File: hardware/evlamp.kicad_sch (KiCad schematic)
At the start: 21 parts

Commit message: update KiCad project
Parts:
- added C2: (no value), symbol GOST_Capacitors:CAPACITOR_POLAR
- C1: value (none) -> 1,0; footprint (none) -> Capacitor_SMD:C_0805_2012Metric_Pad1.18x1.45mm_HandSolder
- X1: footprint (none) -> TerminalBlock:TerminalBlock_bornier-3_P5.08mm
- X11: footprint (none) -> Connector_PinHeader_2.54mm:PinHeader_1x03_P2.54mm_Vertical
- X2: footprint (none) -> TerminalBlock:TerminalBlock_bornier-2_P5.08mm
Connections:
- net +5V: now also C2.1
- net GND: now also C2.2
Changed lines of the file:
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@@
   (junction (at 72.39 114.3) (diameter 0) (color 0 0 0 0)
+  )
+  (junction (at 64.77 106.68) (diameter 0) (color 0 0 0 0)
   )
   (junction (at 72.39 111.76) (diameter 0) (color 0 0 0 0)
@@
     (stroke (width 0) (type default) (color 0 0 0 0))
   )
+  (wire (pts (xy 64.77 106.68) (xy 72.39 106.68))
+    (stroke (width 0) (type default) (color 0 0 0 0))
+  )
   (wire (pts (xy 182.88 76.2) (xy 191.77 76.2))
     (stroke (width 0) (type default) (color 0 0 0 0))
@@
     (stroke (width 0) (type default) (color 0 0 0 0))
   )
+  (wire (pts (xy 62.23 106.68) (xy 64.77 106.68))
+    (stroke (width 0) (type default) (color 0 0 0 0))
+  )
   (wire (pts (xy 124.46 99.06) (xy 129.54 99.06))
     (stroke (width 0) (type default) (color 0 0 0 0))
@@
   )
   (wire (pts (xy 172.72 106.68) (xy 175.26 106.68))
+    (stroke (width 0) (type default) (color 0 0 0 0))
+  )
+  (wire (pts (xy 64.77 106.68) (xy 64.77 109.22))
     (stroke (width 0) (type default) (color 0 0 0 0))
   )
@@
     (pin "1")
   )
-  (symbol (lib_id "GOST_Power_Symbols:+5V") (at 72.39 106.68 90) (unit 1)
-    (in_bom yes) (on_board yes)
-    (property "Reference" "#PWR0102" (id 0) (at 73.152 106.68 0)
-      (effects (font (size 1.27 1.27)) (justify top) hide)
-    )
-    (property "Value" "+5V" (id 1) (at 69.215 106.68 90)
-      (effects (font (size 1.27 1.27)) (justify left))
-    )
-    (property "Footprint" "" (id 2) (at 72.39 106.68 0)
-      (effects (font (size 0 0)) hide)
-    )
-    (property "Datasheet" "" (id 3) (at 72.39 106.68 0)
+  (symbol (lib_id "GOST_Power_Symbols:+5V") (at 62.23 106.68 90) (unit 1)
+    (in_bom yes) (on_board yes)
+    (property "Reference" "#PWR0102" (id 0) (at 62.992 106.68 0)
+      (effects (font (size 1.27 1.27)) (justify top) hide)
+    )
+    (property "Value" "+5V" (id 1) (at 59.055 106.68 90)
+      (effects (font (size 1.27 1.27)) (justify left))
+    )
+    (property "Footprint" "" (id 2) (at 62.23 106.68 0)
+      (effects (font (size 0 0)) hide)
+    )
+    (property "Datasheet" "" (id 3) (at 62.23 106.68 0)
       (effects (font (size 1.27 1.27)) hide)
     )
@@
     (property "Reference" "X2" (id 0) (at 208.28 37.465 0))
     (property "Value" "" (id 1) (at 208.28 40.005 0))
-    (property "Footprint" "" (id 2) (at 208.915 37.465 0)
+    (property "Footprint" "TerminalBlock:TerminalBlock_bornier-2_P5.08mm" (id 2) (at 208.915 37.465 0)
       (effects (font (size 1.27 1.27)) hide)
     )
@@
     (property "Reference" "X11" (id 0) (at 256.54 51.435 0))
     (property "Value" "" (id 1) (at 256.54 53.975 0))
-    (property "Footprint" "" (id 2) (at 257.175 51.435 0)
+    (property "Footprint" "Connector_PinHeader_2.54mm:PinHeader_1x03_P2.54mm_Vertical" (id 2) (at 257.175 51.435 0)
       (effects (font (size 1.27 1.27)) hide)
     )
@@
       (effects (font (size 1.27 1.27)) (justify top) hide)
     )
-    (property "Value" "" (id 1) (at 69.215 104.14 90)
+    (property "Value" "+3V3" (id 1) (at 69.215 104.14 90)
       (effects (font (size 1.27 1.27)) (justify left))
     )
@@
     (property "Reference" "X1" (id 0) (at 208.28 17.145 0))
     (property "Value" "" (id 1) (at 208.28 19.685 0))
-    (property "Footprint" "" (id 2) (at 208.915 17.145 0)
+    (property "Footprint" "TerminalBlock:TerminalBlock_bornier-3_P5.08mm" (id 2) (at 208.915 17.145 0)
       (effects (font (size 1.27 1.27)) hide)
     )
@@
     (pin "2")
   )
+  (symbol (lib_id "GOST_Capacitors:CAPACITOR_POLAR") (at 64.77 111.76 270) (unit 1)
+    (in_bom yes) (on_board yes) (fields_autoplaced)
+    (property "Reference" "C2" (id 0) (at 61.9506 110.1506 90)
+      (effects (font (size 1.27 1.27)) (justify right))
+    )
+    (property "Value" "" (id 1) (at 61.9506 112.6875 90)
+      (effects (font (size 1.27 1.27)) (justify right))
+    )
+    (property "Footprint" "" (id 2) (at 64.77 111.76 0)
+      (effects (font (size 0 0)) hide)
+    )
+    (property "Datasheet" "" (id 3) (at 64.77 111.76 0)
+      (effects (font (size 1.27 1.27)) hide)
+    )
+    (pin "1")
+    (pin "2")
+  )
   (symbol (lib_id "GOST_Power_Symbols:GND") (at 191.77 78.74 0) (unit 1)
     (in_bom yes) (on_board yes)
@@
       (effects (font (size 1.27 1.27)) (justify bottom))
     )
-    (property "Value" "" (id 1) (at 67.31 63.754 0)
+    (property "Value" "1,0" (id 1) (at 67.31 63.754 0)
       (effects (font (size 1.27 1.27)) (justify top))
     )
-    (property "Footprint" "" (id 2) (at 67.31 60.96 0)
+    (property "Footprint" "Capacitor_SMD:C_0805_2012Metric_Pad1.18x1.45mm_HandSolder" (id 2) (at 67.31 60.96 0)
       (effects (font (size 0 0)) hide)
     )
@@
     (pin "1")
   )
+  (symbol (lib_id "GOST_Power_Symbols:GND") (at 64.77 114.3 0) (unit 1)
+    (in_bom yes) (on_board yes)
+    (property "Reference" "#PWR01" (id 0) (at 64.77 113.538 0)
+      (effects (font (size 1.27 1.27)) (justify bottom) hide)
+    )
+    (property "Value" "GND" (id 1) (at 64.77 117.602 0)
+      (effects (font (size 1.27 1.27)) (justify top) hide)
+    )
+    (property "Footprint" "" (id 2) (at 64.77 114.3 0)
+      (effects (font (size 0 0)) hide)
+    )
+    (property "Datasheet" "" (id 3) (at 64.77 114.3 0)
+      (effects (font (size 1.27 1.27)) hide)
+    )
+    (pin "1")
+  )
   (sheet_instances
     (path "/" (page "1"))
   )
   (symbol_instances
+    (path "/fc90aa7b-5a1a-4828-8d95-c11efe269ebf"
+      (reference "#PWR01") (unit 1) (value "GND") (footprint "")
+    )
     (path "/7654ee7c-a140-4a0e-813b-24a19e1eaa35"
       (reference "#PWR0101") (unit 1) (value "GND") (footprint "")
@@
       (reference "C1") (unit 1) (value "1,0") (footprint "Capacitor_SMD:C_0805_2012Metric_Pad1.18x1.45mm_HandSolder")
     )
+    (path "/be2d597d-89ce-40f4-9140-a947d371c7bd"
+      (reference "C2") (unit 1) (value "470,0 6,3V") (footprint "Capacitor_Tantalum_SMD:CP_EIA-7343-31_Kemet-D_Pad2.25x2.55mm_HandSolder")
+    )
     (path "/4604e592-9b56-46c9-9259-5fb3a446e2cc"
-      (reference "DD1") (unit 1) (value "ESP32-DEVKITC") (footprint "greenhouse:ESP32-DEVKITC")
+      (reference "DD1") (unit 1) (value "ESP32-DEVKITC") (footprint "esp32:ESP32-DEVKITC")
     )
     (path "/200da659-a750-4281-8b29-3ef60e1bd36a"
@@
     )
     (path "/9cf37ab0-58d2-419a-9c76-4836af0b31df"
-      (reference "X1") (unit 1) (value "LED MATRIX 0") (footprint "TerminalBlock:TerminalBlock_bornier-3_P5.08mm")
+      (reference "X1") (unit 1) (value "LED 0") (footprint "TerminalBlock:TerminalBlock_bornier-3_P5.08mm")
     )
     (path "/57296adc-2b68-421f-b53a-73d7e755b961"
-      (reference "X2") (unit 1) (value "LED MATRIX 1") (footprint "TerminalBlock:TerminalBlock_bornier-2_P5.08mm")
+      (reference "X2") (unit 1) (value "LED 1") (footprint "TerminalBlock:TerminalBlock_bornier-2_P5.08mm")
     )
     (path "/b1ac7493-f372-44b1-8938-1ca6234b0e30"
-      (reference "X3") (unit 1) (value "LED MATRIX 2") (footprint "TerminalBlock:TerminalBlock_bornier-2_P5.08mm")
+      (reference "X3") (unit 1) (value "LED 2") (footprint "TerminalBlock:TerminalBlock_bornier-2_P5.08mm")
     )
     (path "/bbc6eae6-9de9-4787-8c91-fa9c911da324"
-      (reference "X4") (unit 1) (value "LED MATRIX 3") (footprint "TerminalBlock:TerminalBlock_bornier-2_P5.08mm")
+      (reference "X4") (unit 1) (value "LED 3") (footprint "TerminalBlock:TerminalBlock_bornier-2_P5.08mm")
     )
     (path "/a6082326-b441-4ae4-a66e-dccfa7bf2440"
-      (reference "X5") (unit 1) (value "LED MATRIX 4") (footprint "TerminalBlock:TerminalBlock_bornier-2_P5.08mm")
+      (reference "X5") (unit 1) (value "LED 4") (footprint "TerminalBlock:TerminalBlock_bornier-2_P5.08mm")
     )
     (path "/5ab0c5b9-6610-4c6e-8b25-117e8f555b6a"
-      (reference "X6") (unit 1) (value "LED MATRIX 5") (footprint "TerminalBlock:TerminalBlock_bornier-2_P5.08mm")
+      (reference "X6") (unit 1) (value "LED 5") (footprint "TerminalBlock:TerminalBlock_bornier-2_P5.08mm")
     )
     (path "/84330340-6bca-4e71-b878-05a562b1af7b"
-      (reference "X7") (unit 1) (value "LED MATRIX 6") (footprint "TerminalBlock:TerminalBlock_bornier-2_P5.08mm")
+      (reference "X7") (unit 1) (value "LED 6") (footprint "TerminalBlock:TerminalBlock_bornier-2_P5.08mm")
     )
     (path "/dfaab0c3-5ddf-43d3-9277-3ae5c0732dc5"
-      (reference "X8") (unit 1) (value "LED MATRIX 7") (footprint "TerminalBlock:TerminalBlock_bornier-2_P5.08mm")
+      (reference "X8") (unit 1) (value "LED 7") (footprint "TerminalBlock:TerminalBlock_bornier-2_P5.08mm")
     )
     (path "/f15ee583-977e-4cfd-9cf5-6b3a3925b159"
-      (reference "X9") (unit 1) (value "UP BUTTON") (footprint "Connector_PinHeader_2.54mm:PinHeader_1x03_P2.54mm_Vertical")
+      (reference "X9") (unit 1) (value "\"UP\"") (footprint "Connector_PinHeader_2.54mm:PinHeader_1x03_P2.54mm_Vertical")
     )
     (path "/4c44a65f-925f-4d4b-88e3-40d0fa1c9329"
-      (reference "X10") (unit 1) (value "DOWN BUTTON") (footprint "Connector_PinHeader_2.54mm:PinHeader_1x03_P2.54mm_Vertical")
+      (reference "X10") (unit 1) (value "\"DOWN\"") (footprint "Connector_PinHeader_2.54mm:PinHeader_1x03_P2.54mm_Vertical")
     )
     (path "/5a0dc42c-ea51-4df6-9cc3-e6b60f3d39be"
-      (reference "X11") (unit 1) (value "MAIN BUTTON") (footprint "Connector_PinHeader_2.54mm:PinHeader_1x03_P2.54mm_Vertical")
-    )
-  )
+      (reference "X11") (unit 1) (value "\"MAIN\"") (footprint "Connector_PinHeader_2.54mm:PinHeader_1x03_P2.54mm_Vertical")
+    )
+  )

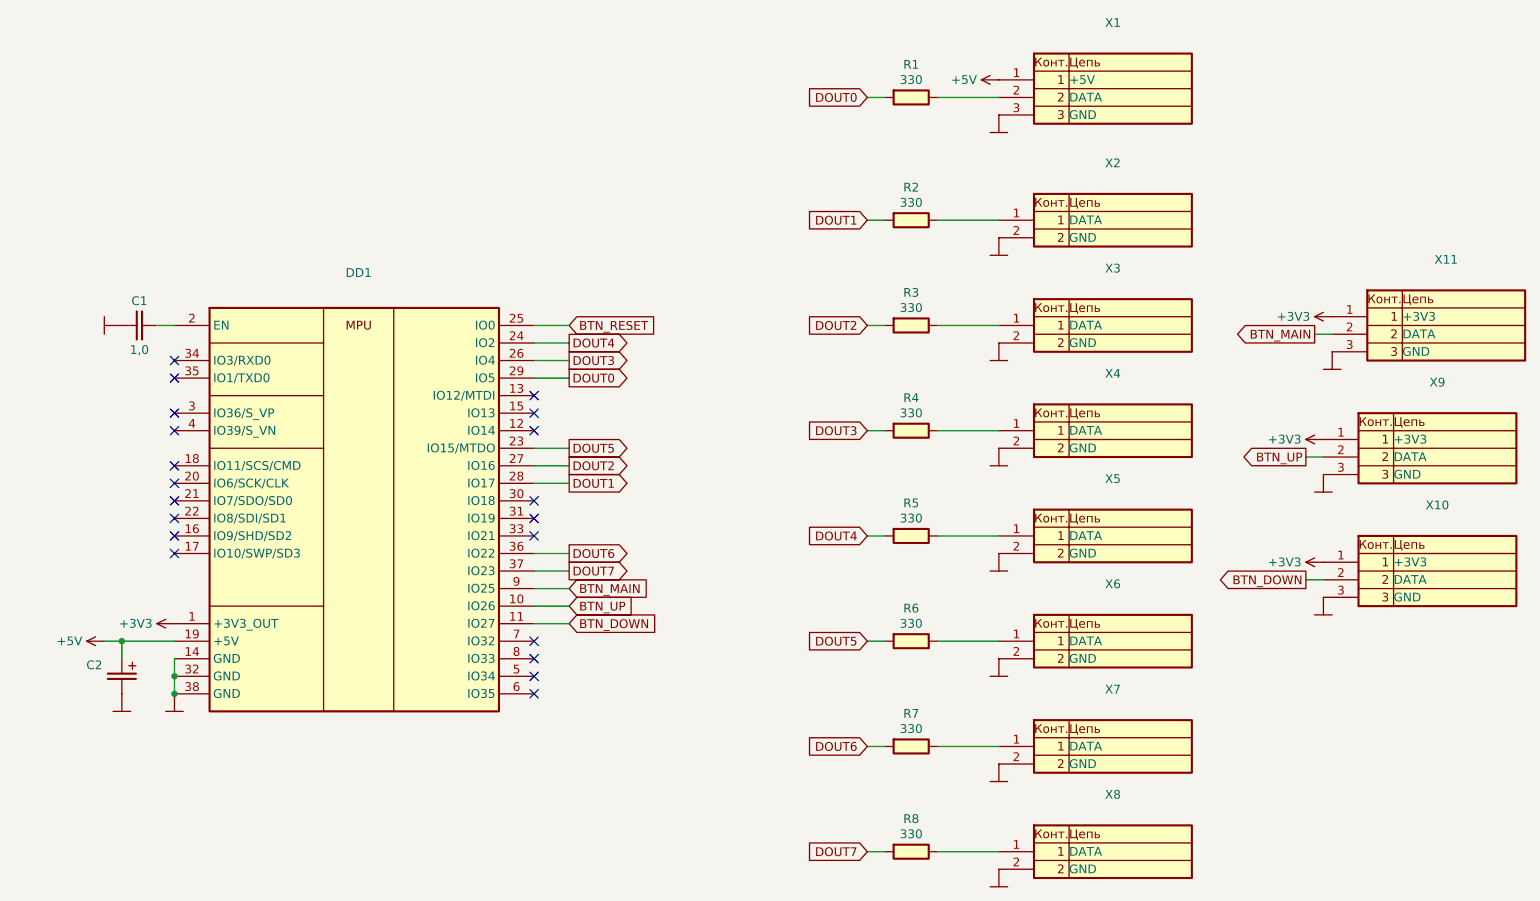
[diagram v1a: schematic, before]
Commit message: add checkbox support to effect parameters
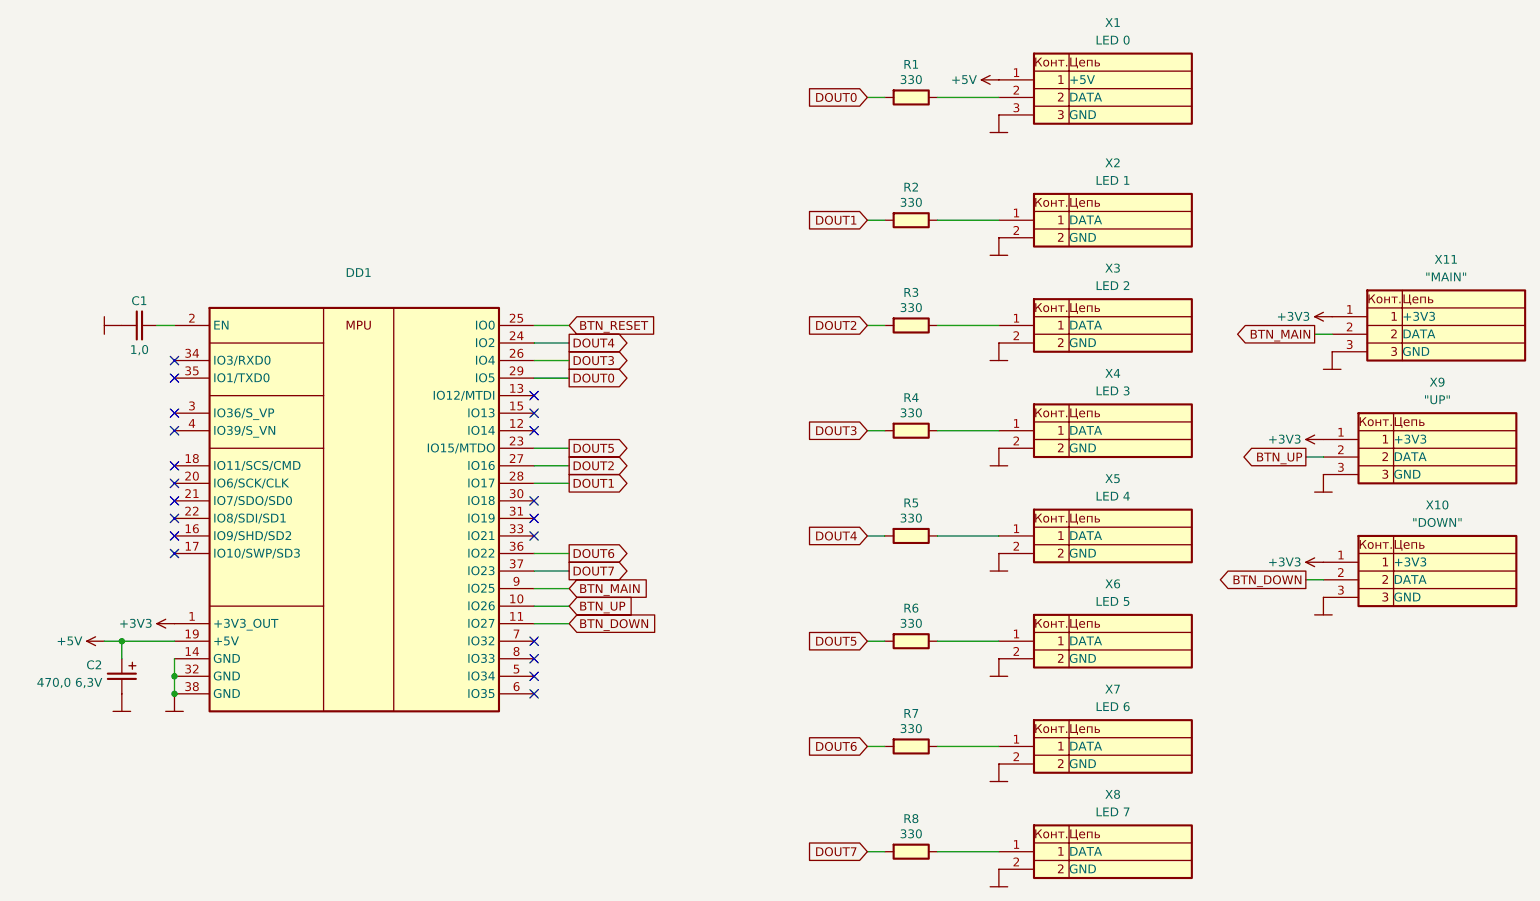
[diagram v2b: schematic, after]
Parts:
- C2: value (none) -> 470,0 6,3V; footprint (none) -> Capacitor_Tantalum_SMD:CP_EIA-7343-31_Kemet-D_Pad2.25x2.55mm_HandSolder
- X1: value (none) -> LED 0
- X10: value (none) -> "DOWN"
- X11: value (none) -> "MAIN"
- X2: value (none) -> LED 1
- X3: value (none) -> LED 2
- X4: value (none) -> LED 3
- X5: value (none) -> LED 4
- X6: value (none) -> LED 5
- X7: value (none) -> LED 6
- X8: value (none) -> LED 7
- X9: value (none) -> "UP"
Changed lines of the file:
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@@
     (in_bom yes) (on_board yes)
     (property "Reference" "X10" (id 0) (at 255.27 86.995 0))
-    (property "Value" "" (id 1) (at 255.27 89.535 0))
+    (property "Value" "\"DOWN\"" (id 1) (at 255.27 89.535 0))
     (property "Footprint" "Connector_PinHeader_2.54mm:PinHeader_1x03_P2.54mm_Vertical" (id 2) (at 255.905 86.995 0)
       (effects (font (size 1.27 1.27)) hide)
@@
     (in_bom yes) (on_board yes)
     (property "Reference" "X2" (id 0) (at 208.28 37.465 0))
-    (property "Value" "" (id 1) (at 208.28 40.005 0))
+    (property "Value" "LED 1" (id 1) (at 208.28 40.005 0))
     (property "Footprint" "TerminalBlock:TerminalBlock_bornier-2_P5.08mm" (id 2) (at 208.915 37.465 0)
       (effects (font (size 1.27 1.27)) hide)
@@
     (in_bom yes) (on_board yes)
     (property "Reference" "X11" (id 0) (at 256.54 51.435 0))
-    (property "Value" "" (id 1) (at 256.54 53.975 0))
+    (property "Value" "\"MAIN\"" (id 1) (at 256.54 53.975 0))
     (property "Footprint" "Connector_PinHeader_2.54mm:PinHeader_1x03_P2.54mm_Vertical" (id 2) (at 257.175 51.435 0)
       (effects (font (size 1.27 1.27)) hide)
@@
     (in_bom yes) (on_board yes)
     (property "Reference" "X6" (id 0) (at 208.28 98.425 0))
-    (property "Value" "" (id 1) (at 208.28 100.965 0))
+    (property "Value" "LED 5" (id 1) (at 208.28 100.965 0))
     (property "Footprint" "TerminalBlock:TerminalBlock_bornier-2_P5.08mm" (id 2) (at 208.915 98.425 0)
       (effects (font (size 1.27 1.27)) hide)
@@
     (in_bom yes) (on_board yes)
     (property "Reference" "X7" (id 0) (at 208.28 113.665 0))
-    (property "Value" "" (id 1) (at 208.28 116.205 0))
+    (property "Value" "LED 6" (id 1) (at 208.28 116.205 0))
     (property "Footprint" "TerminalBlock:TerminalBlock_bornier-2_P5.08mm" (id 2) (at 208.915 113.665 0)
       (effects (font (size 1.27 1.27)) hide)
@@
     (in_bom yes) (on_board yes)
     (property "Reference" "X1" (id 0) (at 208.28 17.145 0))
-    (property "Value" "" (id 1) (at 208.28 19.685 0))
+    (property "Value" "LED 0" (id 1) (at 208.28 19.685 0))
     (property "Footprint" "TerminalBlock:TerminalBlock_bornier-3_P5.08mm" (id 2) (at 208.915 17.145 0)
       (effects (font (size 1.27 1.27)) hide)
@@
     (in_bom yes) (on_board yes)
     (property "Reference" "X5" (id 0) (at 208.28 83.185 0))
-    (property "Value" "" (id 1) (at 208.28 85.725 0))
+    (property "Value" "LED 4" (id 1) (at 208.28 85.725 0))
     (property "Footprint" "TerminalBlock:TerminalBlock_bornier-2_P5.08mm" (id 2) (at 208.915 83.185 0)
       (effects (font (size 1.27 1.27)) hide)
@@
     (in_bom yes) (on_board yes)
     (property "Reference" "X3" (id 0) (at 208.28 52.705 0))
-    (property "Value" "" (id 1) (at 208.28 55.245 0))
+    (property "Value" "LED 2" (id 1) (at 208.28 55.245 0))
     (property "Footprint" "TerminalBlock:TerminalBlock_bornier-2_P5.08mm" (id 2) (at 208.915 52.705 0)
       (effects (font (size 1.27 1.27)) hide)
@@
     (in_bom yes) (on_board yes)
     (property "Reference" "X4" (id 0) (at 208.28 67.945 0))
-    (property "Value" "" (id 1) (at 208.28 70.485 0))
+    (property "Value" "LED 3" (id 1) (at 208.28 70.485 0))
     (property "Footprint" "TerminalBlock:TerminalBlock_bornier-2_P5.08mm" (id 2) (at 208.915 67.945 0)
       (effects (font (size 1.27 1.27)) hide)
@@
       (effects (font (size 1.27 1.27)) (justify right))
     )
-    (property "Value" "" (id 1) (at 61.9506 112.6875 90)
+    (property "Value" "470,0 6,3V" (id 1) (at 61.9506 112.6875 90)
       (effects (font (size 1.27 1.27)) (justify right))
     )
-    (property "Footprint" "" (id 2) (at 64.77 111.76 0)
+    (property "Footprint" "Capacitor_Tantalum_SMD:CP_EIA-7343-31_Kemet-D_Pad2.25x2.55mm_HandSolder" (id 2) (at 64.77 111.76 0)
       (effects (font (size 0 0)) hide)
     )
@@
     (in_bom yes) (on_board yes)
     (property "Reference" "X8" (id 0) (at 208.28 128.905 0))
-    (property "Value" "" (id 1) (at 208.28 131.445 0))
+    (property "Value" "LED 7" (id 1) (at 208.28 131.445 0))
     (property "Footprint" "TerminalBlock:TerminalBlock_bornier-2_P5.08mm" (id 2) (at 208.915 128.905 0)
       (effects (font (size 1.27 1.27)) hide)
@@
     (in_bom yes) (on_board yes)
     (property "Reference" "X9" (id 0) (at 255.27 69.215 0))
-    (property "Value" "" (id 1) (at 255.27 71.755 0))
+    (property "Value" "\"UP\"" (id 1) (at 255.27 71.755 0))
     (property "Footprint" "Connector_PinHeader_2.54mm:PinHeader_1x03_P2.54mm_Vertical" (id 2) (at 255.905 69.215 0)
       (effects (font (size 1.27 1.27)) hide)

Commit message: update to ver 0.7.4
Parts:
- DD1: value (none) -> ESP32-DEVKITC; footprint (none) -> esp32:ESP32-DEVKITC
